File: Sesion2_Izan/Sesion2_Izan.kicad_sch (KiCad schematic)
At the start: 0 parts

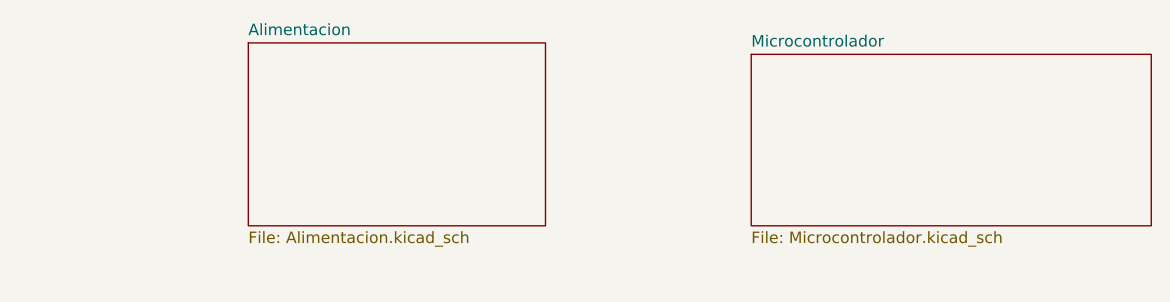
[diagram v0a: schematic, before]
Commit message: Complete power supply schematic
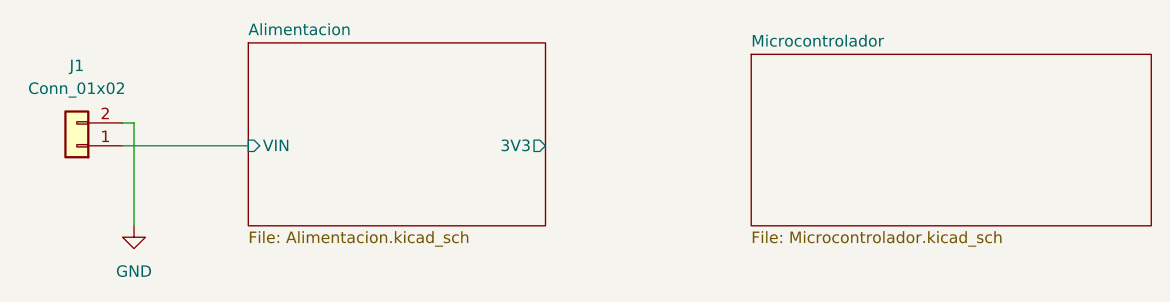
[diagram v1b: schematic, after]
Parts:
- added J1: Conn_01x02, TerminalBlock_Phoenix:TerminalBlock_Phoenix_PT-1,5-2-5.0-H_1x02_P5.00mm_Horizontal, symbol Connector_Generic:Conn_01x02
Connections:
- new net Alimentacion/VIN: J1.1 (Pin_1)
- new net GND: J1.2 (Pin_2)
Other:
- sheet Alimentacion ports: added 3V3, VIN; removed none
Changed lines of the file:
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@@
 	(generator_version "10.0")
 	(paper "A4")
+	(wire
+		(pts
+			(xy 29.21 97.79) (xy 30.48 97.79)
+		)
+		(stroke
+			(width 0)
+			(type default)
+		)
+	)
+	(wire
+		(pts
+			(xy 30.48 97.79) (xy 30.48 109.22)
+		)
+		(stroke
+			(width 0)
+			(type default)
+		)
+	)
+	(wire
+		(pts
+			(xy 29.21 100.33) (xy 43.18 100.33)
+		)
+		(stroke
+			(width 0)
+			(type default)
+		)
+	)
+	(symbol
+		(lib_id "Connector_Generic:Conn_01x02")
+		(at 24.13 100.33 180)
+		(unit 1)
+		(body_style 1)
+		(exclude_from_sim no)
+		(in_bom yes)
+		(on_board yes)
+		(in_pos_files yes)
+		(dnp no)
+		(fields_autoplaced yes)
+		(property "Reference" "J1"
+			(at 24.13 91.44 0)
+			(show_name no)
+			(do_not_autoplace no)
+			(effects
+				(font
+					(size 1.27 1.27)
+				)
+			)
+		)
+		(property "Value" "Conn_01x02"
+			(at 24.13 93.98 0)
+			(show_name no)
+			(do_not_autoplace no)
+			(effects
+				(font
+					(size 1.27 1.27)
+				)
+			)
+		)
+		(property "Footprint" "TerminalBlock_Phoenix:TerminalBlock_Phoenix_PT-1,5-2-5.0-H_1x02_P5.00mm_Horizontal"
+			(at 24.13 100.33 0)
+			(hide yes)
+			(show_name no)
+			(do_not_autoplace no)
+			(effects
+				(font
+					(size 1.27 1.27)
+				)
+			)
+		)
+		(property "Datasheet" ""
+			(at 24.13 100.33 0)
+			(hide yes)
+			(show_name no)
+			(do_not_autoplace no)
+			(effects
+				(font
+					(size 1.27 1.27)
+				)
+			)
+		)
+		(property "Description" "Generic connector, single row, 01x02, script generated (kicad-library-utils/schlib/autogen/connector/)"
+			(at 24.13 100.33 0)
+			(hide yes)
+			(show_name no)
+			(do_not_autoplace no)
+			(effects
+				(font
+					(size 1.27 1.27)
+				)
+			)
+		)
+		(property "Manufacturer" "Phoenix Contact"
+			(at 24.13 100.33 0)
+			(hide yes)
+			(show_name no)
+			(do_not_autoplace no)
+			(effects
+				(font
+					(size 1.27 1.27)
+				)
+			)
+		)
+		(property "MPN" "1935161"
+			(at 24.13 100.33 0)
+			(hide yes)
+			(show_name no)
+			(do_not_autoplace no)
+			(effects
+				(font
+					(size 1.27 1.27)
+				)
+			)
+		)
+		(pin "1"
+		)
+		(pin "2"
+		)
+		(instances
+			(project "Sesion2_Izan"
+				(path "/e349a083-9e3b-40e5-ab26-55c4e44866b1"
+					(reference "J1")
+					(unit 1)
+				)
+			)
+		)
+	)
+	(symbol
+		(lib_id "power:GND")
+		(at 30.48 109.22 0)
+		(unit 1)
+		(body_style 1)
+		(exclude_from_sim no)
+		(in_bom yes)
+		(on_board yes)
+		(in_pos_files yes)
+		(dnp no)
+		(fields_autoplaced yes)
+		(property "Reference" "#PWR04"
+			(at 30.48 115.57 0)
+			(hide yes)
+			(show_name no)
+			(do_not_autoplace no)
+			(effects
+				(font
+					(size 1.27 1.27)
+				)
+			)
+		)
+		(property "Value" "GND"
+			(at 30.48 114.3 0)
+			(show_name no)
+			(do_not_autoplace no)
+			(effects
+				(font
+					(size 1.27 1.27)
+				)
+			)
+		)
+		(property "Footprint" ""
+			(at 30.48 109.22 0)
+			(hide yes)
+			(show_name no)
+			(do_not_autoplace no)
+			(effects
+				(font
+					(size 1.27 1.27)
+				)
+			)
+		)
+		(property "Datasheet" ""
+			(at 30.48 109.22 0)
+			(hide yes)
+			(show_name no)
+			(do_not_autoplace no)
+			(effects
+				(font
+					(size 1.27 1.27)
+				)
+			)
+		)
+		(property "Description" "Power symbol creates a global label with name \"GND\" , ground"
+			(at 30.48 109.22 0)
+			(hide yes)
+			(show_name no)
+			(do_not_autoplace no)
+			(effects
+				(font
+					(size 1.27 1.27)
+				)
+			)
+		)
+		(pin "1"
+		)
+		(instances
+			(project "Sesion2_Izan"
+				(path "/e349a083-9e3b-40e5-ab26-55c4e44866b1"
+					(reference "#PWR04")
+					(unit 1)
+				)
+			)
+		)
+	)
 	(sheet
 		(at 99.06 90.17)
@@
 			)
 		)
+		(pin "3V3" output
+			(at 76.2 100.33 0)
+			(effects
+				(font
+					(size 1.27 1.27)
+				)
+				(justify right)
+			)
+		)
+		(pin "VIN" input
+			(at 43.18 100.33 180)
+			(effects
+				(font
+					(size 1.27 1.27)
+				)
+				(justify left)
+			)
+		)
